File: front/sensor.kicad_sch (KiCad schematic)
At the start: 1 part, among them U1 VL53L8CXV0GC/1

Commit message: start adding components
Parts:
- removed U1: VL53L8CXV0GC/1, Library:IC17_LGA16_STM, symbol New_Library:VL53L8CXV0GC_1
- added U2: VL53L8CXV0GC/1, Library:IC17_LGA16_STM, symbol New_Library:VL53L8CXV0GC_1
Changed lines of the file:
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@@
 	(symbol
 		(lib_id "New_Library:VL53L8CXV0GC_1")
-		(at 113.03 85.09 0)
+		(at 121.92 87.63 0)
 		(unit 1)
 		(exclude_from_sim no)
@@
 		(dnp no)
 		(fields_autoplaced yes)
-		(property "Reference" "U1"
-			(at 143.51 74.93 0)
+		(property "Reference" "U2"
+			(at 152.4 77.47 0)
 			(effects
 				(font
@@
 		)
 		(property "Value" "VL53L8CXV0GC/1"
-			(at 143.51 77.47 0)
+			(at 152.4 80.01 0)
 			(effects
 				(font
@@
 		)
 		(property "Footprint" "Library:IC17_LGA16_STM"
-			(at 113.03 85.09 0)
+			(at 121.92 87.63 0)
 			(effects
 				(font
@@
 		)
 		(property "Datasheet" "https://www.st.com/resource/en/datasheet/vl53l8cx.pdf"
-			(at 113.03 85.09 0)
+			(at 121.92 87.63 0)
 			(effects
 				(font
@@
 		)
 		(property "Description" ""
-			(at 113.03 85.09 0)
+			(at 121.92 87.63 0)
 			(effects
 				(font
@@
 			)
 		)
-		(pin "B1"
+		(pin "C1"
+		)
+		(pin "A5"
+		)
+		(pin "C7"
 		)
 		(pin "C2"
 		)
-		(pin "C3"
-		)
-		(pin "C5"
-		)
-		(pin "A3"
-		)
-		(pin "A4"
+		(pin "C4"
 		)
 		(pin "B7"
-		)
-		(pin "C7"
-		)
-		(pin "A5"
-		)
-		(pin "A6"
-		)
-		(pin "A7"
-		)
-		(pin "C4"
 		)
 		(pin "B4"
@@
 		(pin "A2"
 		)
-		(pin "C1"
+		(pin "A4"
 		)
 		(pin "A1"
 		)
+		(pin "A3"
+		)
+		(pin "A6"
+		)
+		(pin "B1"
+		)
+		(pin "C3"
+		)
+		(pin "A7"
+		)
 		(pin "C6"
+		)
+		(pin "C5"
 		)
 		(instances
 			(project ""
-				(path "/b2652d05-715e-42f8-8ce3-856452645a23"
-					(reference "U1")
+				(path "/508f986b-6f1b-4c39-bd57-bae69573a4e7/0b3f6a80-597d-49fc-a7c3-ab9dba8221cb"
+					(reference "U2")
 					(unit 1)
 				)
@@
 		)
 	)
-	(sheet_instances
-		(path "/"
-			(page "1")
-		)
-	)
-	(embedded_fonts no)
 )

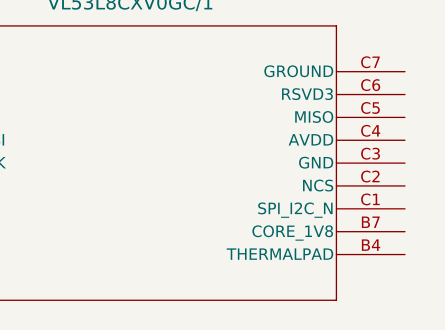
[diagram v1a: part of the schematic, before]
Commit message: add some traces
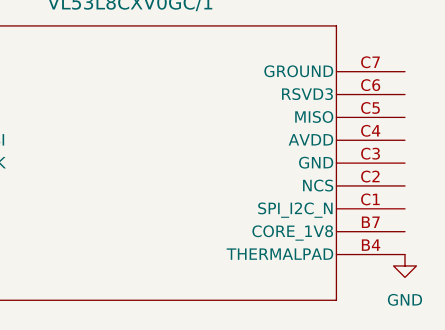
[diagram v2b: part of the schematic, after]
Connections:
- net GND: now reaches U2.B4 (THERMALPAD)
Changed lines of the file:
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@@
 	(paper "A4")
+	(symbol
+		(lib_id "power:GND")
+		(at 182.88 107.95 0)
+		(unit 1)
+		(exclude_from_sim no)
+		(in_bom yes)
+		(on_board yes)
+		(dnp no)
+		(fields_autoplaced yes)
+		(property "Reference" "#PWR02"
+			(at 182.88 114.3 0)
+			(effects
+				(font
+					(size 1.27 1.27)
+				)
+				(hide yes)
+			)
+		)
+		(property "Value" "GND"
+			(at 182.88 113.03 0)
+			(effects
+				(font
+					(size 1.27 1.27)
+				)
+			)
+		)
+		(property "Footprint" ""
+			(at 182.88 107.95 0)
+			(effects
+				(font
+					(size 1.27 1.27)
+				)
+				(hide yes)
+			)
+		)
+		(property "Datasheet" ""
+			(at 182.88 107.95 0)
+			(effects
+				(font
+					(size 1.27 1.27)
+				)
+				(hide yes)
+			)
+		)
+		(property "Description" "Power symbol creates a global label with name \"GND\" , ground"
+			(at 182.88 107.95 0)
+			(effects
+				(font
+					(size 1.27 1.27)
+				)
+				(hide yes)
+			)
+		)
+		(pin "1"
+		)
+		(instances
+			(project ""
+				(path "/508f986b-6f1b-4c39-bd57-bae69573a4e7/0b3f6a80-597d-49fc-a7c3-ab9dba8221cb"
+					(reference "#PWR02")
+					(unit 1)
+				)
+			)
+		)
+	)
 	(symbol
 		(lib_id "New_Library:VL53L8CXV0GC_1")

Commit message: add more components
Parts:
- added C2, C3: 100n, Capacitor_SMD:C_0603_1608Metric, symbol Device:C
- added C4: 4.7u, Capacitor_SMD:C_0603_1608Metric, symbol Device:C
- added C8: 10u, Capacitor_SMD:C_0603_1608Metric, symbol Device:C
- added C9: 1u, Capacitor_SMD:C_0603_1608Metric, symbol Device:C
- added J4: Conn_01x04_Pin, Connector_PinHeader_2.54mm:PinHeader_1x04_P2.54mm_Horizontal, symbol Connector:Conn_01x04_Pin
- added R1, R2, R3, R4, R5: 47k, Resistor_SMD:R_0603_1608Metric, symbol Device:R
- added R6, R7: R, Resistor_SMD:R_0603_1608Metric, symbol Device:R
- added U5: LDK130M18R, Library:SOT23-5L_1P75X3P05X0P95_STM, symbol New_Library:LDK130M18R
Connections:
- net GND: now also U2.A6 (RSVD1), U2.A7 (RSVD2), U2.C3 (GND), U2.C6 (RSVD3), U2.C7 (GROUND), C2.2, C3.2, C4.2, C8.2, C9.2, J4.2 (Pin_2), R1.2, R3.1, U5.2 (GND)
- net at U2.A1 (INT): now also R2.2
- net at U2.A2 (LPN): now also R4.2
- net 1.8v: now reaches U2.A3 (IOVDD)
- net 1.8v: now also U2.B7 (CORE_1V8), C2.1, C3.1, C8.1, R2.1, R4.1, R5.2, R6.2, R7.2, U5.5 (OUT)
- net sd_vl: now reaches U2.A4 (SDA/MOSI)
- net sd_vl: now also J4.3 (Pin_3), R7.1
- net sc_vl: now reaches U2.A5 (SCL/MCLK)
- net sc_vl: now also J4.4 (Pin_4), R6.1
- net at U2.B1 (SYNC): now also R5.1
- net at U2.C1 (SPI_I2C_N): now also R3.2
- net at U2.C2 (NCS): now also R1.1
- net 3.3v: now reaches U2.C4 (AVDD)
- net 3.3v: now also C4.1, C9.1, J4.1 (Pin_1), U5.1 (IN), U5.3 (EN)
- no-connect marks 0 -> 2
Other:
- note added: "LDK130M18R"

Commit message: begin layout
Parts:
- removed C8: 10u, Capacitor_SMD:C_0603_1608Metric, symbol Device:C
- removed C9: 1u, Capacitor_SMD:C_0603_1608Metric, symbol Device:C
- removed U5: LDK130M18R, Library:SOT23-5L_1P75X3P05X0P95_STM, symbol New_Library:LDK130M18R
- C2, C3, C4, R1, R2, R3, R4, R5, R6, R7, U2: QTY_MULTIPLIER (none) -> 3
- J4: value Conn_01x04_Pin -> Conn_01x05_Pin; footprint Connector_PinHeader_2.54mm:PinHeader_1x04_P2.54mm_Horizontal -> Connector_PinHeader_2.54mm:PinHeader_1x05_P2.54mm_Horizontal; symbol Connector:Conn_01x04_Pin -> Connector:Conn_01x05_Pin; QTY_MULTIPLIER (none) -> 3
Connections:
- net 1.8v: now also J4.5 (Pin_5)
- net 3.3v: now also J4.2 (Pin_2); no longer J4.1 (Pin_1)
- net GND: now also J4.1 (Pin_1); no longer J4.2 (Pin_2)
- net sc_vl: now also J4.3 (Pin_3); no longer J4.4 (Pin_4)
- net sd_vl: now also J4.4 (Pin_4); no longer J4.3 (Pin_3)
- no-connect marks 2 -> 1
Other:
- note removed: "LDK130M18R"

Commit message: push changes
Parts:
- R7: value R -> 2k
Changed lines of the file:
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@@
 			)
 		)
-		(property "Value" "R"
+		(property "Value" "2k"
 			(at 134.62 71.374 90)
 			(show_name no)
